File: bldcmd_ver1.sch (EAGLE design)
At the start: 94 parts, among them CN1 DF61-2P-2.2V(23), IC1 STSPIN32F0, IC2 AS5047P-ATSM, IC3 ADM4852ACPZ-REEL7, J1 DF65-3P-1.7V(21), Q1 PSMN2R4-30MLD, Q2 PSMN2R4-30MLD, Q3 PSMN2R4-30MLD, Q4 PSMN2R4-30MLD, Q5 PSMN2R4-30MLD, Q6 PSMN2R4-30MLD, SW1 SKRP

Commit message: DF65のライブラリ場所の変更を適用
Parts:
- CN1: device SamacSys_Parts:DF61-2P-2.2V(23) -> scramble-con-hirose:DF61-2P-2.2V(23)
- J1: device rcssl_lib:DF65-3P-1.7V(21) -> scramble-con-hirose:DF65-3P-1.7V(21)
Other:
- moved on the sheet: J1
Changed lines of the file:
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@@
 <part name="C11" library="rcl" library_urn="urn:adsk.eagle:library:334" deviceset="C-EU" device="C1206K" package3d_urn="urn:adsk.eagle:package:23682/2" value="47u"/>
 <part name="SUPPLY10" library="supply2" library_urn="urn:adsk.eagle:library:372" deviceset="GND" device=""/>
-<part name="J1" library="rcssl_lib" deviceset="DF65-3P-1.7V(21)" device=""/>
+<part name="J1" library="scramble-con-hirose" deviceset="DF65-3P-1.7V(21)" device=""/>
 <part name="D1" library="diode" library_urn="urn:adsk.eagle:library:210" deviceset="SMF5.0AT1" device="" package3d_urn="urn:adsk.eagle:package:43458/1"/>
 <part name="C12" library="rcl" library_urn="urn:adsk.eagle:library:334" deviceset="C-EU" device="C0603K" package3d_urn="urn:adsk.eagle:package:23680/2" value="0.1u"/>
@@
 <part name="H7" library="holes" library_urn="urn:adsk.eagle:library:237" deviceset="MOUNT-HOLE" device="3.2" package3d_urn="urn:adsk.eagle:package:14275/1"/>
 <part name="H8" library="holes" library_urn="urn:adsk.eagle:library:237" deviceset="MOUNT-HOLE" device="3.2" package3d_urn="urn:adsk.eagle:package:14275/1"/>
-<part name="CN1" library="SamacSys_Parts" deviceset="DF61-2P-2.2V(23)" device=""/>
+<part name="CN1" library="scramble-con-hirose" deviceset="DF61-2P-2.2V(23)" device=""/>
 </parts>
 <sheets>
@@
 <instance part="H7" gate="G$1" x="111.76" y="83.82"/>
 <instance part="H8" gate="G$1" x="111.76" y="88.9"/>
-<instance part="CN1" gate="G$1" x="83.82" y="81.28" rot="MR180"/>
+<instance part="CN1" gate="G$1" x="86.36" y="78.74" rot="MR180"/>
 </instances>
 <busses>
@@
 <wire x1="76.2" y1="78.74" x2="76.2" y2="76.2" width="0.1524" layer="91"/>
 <pinref part="CN1" gate="G$1" pin="1"/>
-<wire x1="78.74" y1="78.74" x2="76.2" y2="78.74" width="0.1524" layer="91"/>
+<wire x1="76.2" y1="78.74" x2="86.36" y2="78.74" width="0.1524" layer="91"/>
 </segment>
 </net>
@@
 <wire x1="76.2" y1="81.28" x2="76.2" y2="83.82" width="0.1524" layer="91"/>
 <pinref part="CN1" gate="G$1" pin="2"/>
-<wire x1="78.74" y1="81.28" x2="76.2" y2="81.28" width="0.1524" layer="91"/>
+<wire x1="76.2" y1="81.28" x2="86.36" y2="81.28" width="0.1524" layer="91"/>
 </segment>
 </net>
@@
 <instance part="R13" gate="G$1" x="96.52" y="22.86" rot="R90"/>
 <instance part="SUPPLY1" gate="GND" x="96.52" y="10.16"/>
-<instance part="J1" gate="G$1" x="236.22" y="55.88" rot="MR180"/>
+<instance part="J1" gate="G$1" x="236.22" y="58.42" rot="MR180"/>
 <instance part="P+2" gate="1" x="96.52" y="96.52"/>
 </instances>

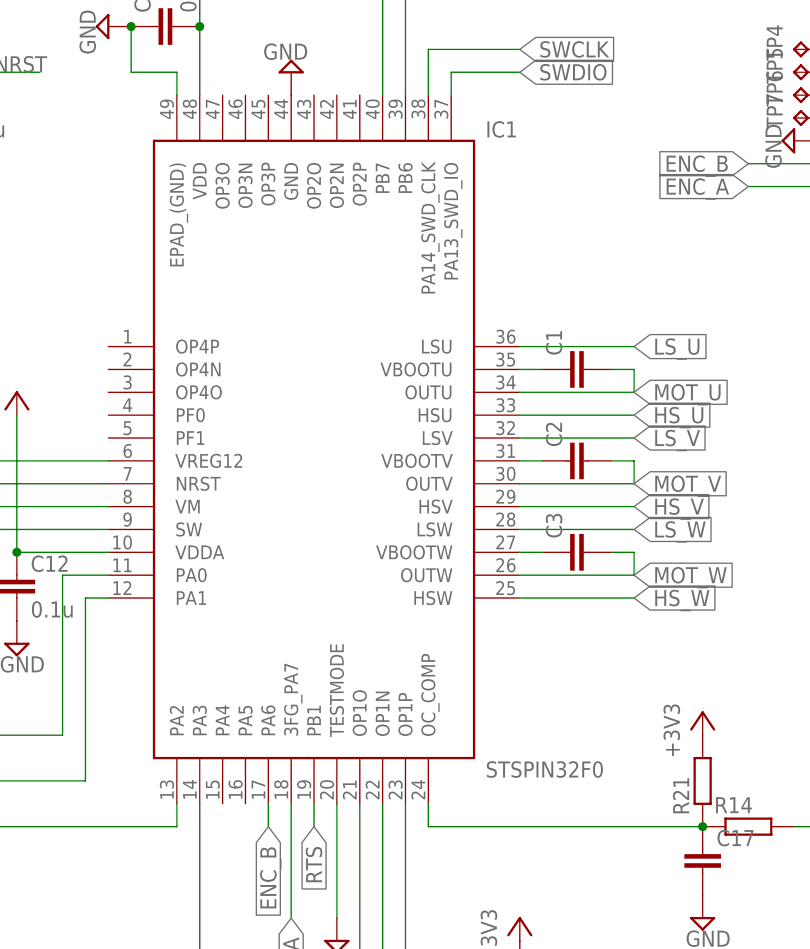
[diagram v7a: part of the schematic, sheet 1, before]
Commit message: #2 の対応，MCUをstspin32F0Aに変更
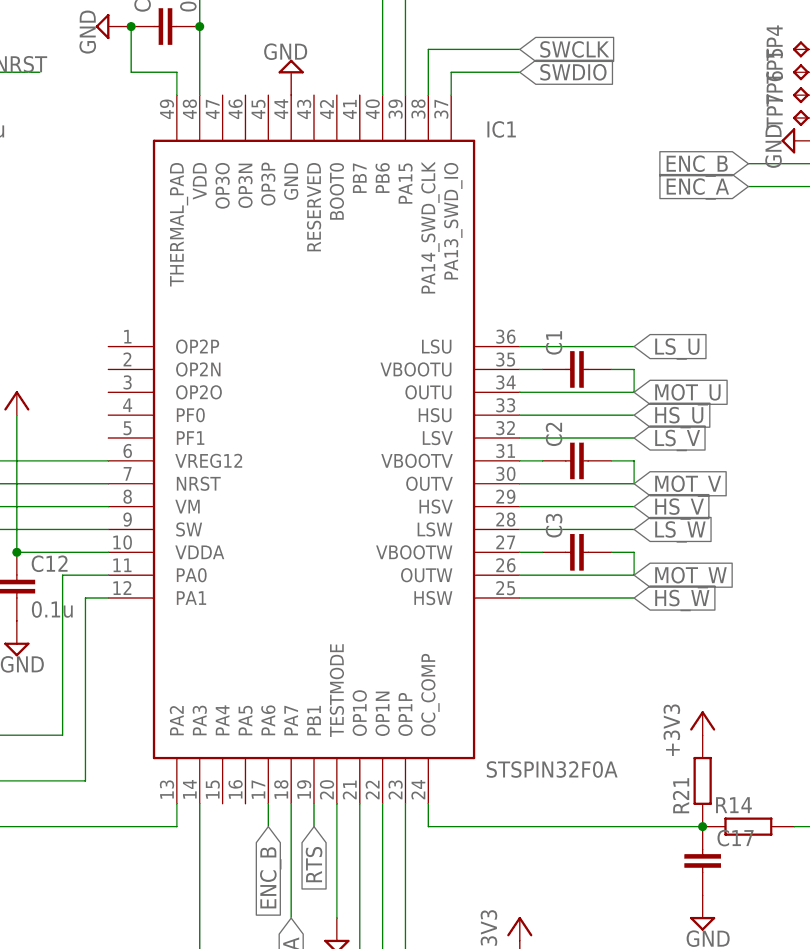
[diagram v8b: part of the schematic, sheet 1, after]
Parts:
- IC1: value STSPIN32F0 -> STSPIN32F0A; device rcssl_lib:STSPIN32F0 -> scramble-mcu:STSPIN32F0A
- renumbered J1 to CN2
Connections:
- net ENC_A: now also IC1.PA7; no longer IC1.3FG_PA7
- net GND: now also IC1.THERMAL_PAD; no longer IC1.EPAD_(GND)
- net UART_RX: now also IC1.PB6; no longer IC1.PB7
- net UART_TX: now also IC1.PA15; no longer IC1.PB6
